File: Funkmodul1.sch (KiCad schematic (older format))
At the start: 54 parts, among them Q1 SSM3J334RLFTR-ND, Q17 AO3414, Q2 AO3414, U1 MC74HC4538A, U2 MAX892, U3 ATMEGA128-16AU, Y1 407F39D007M3728

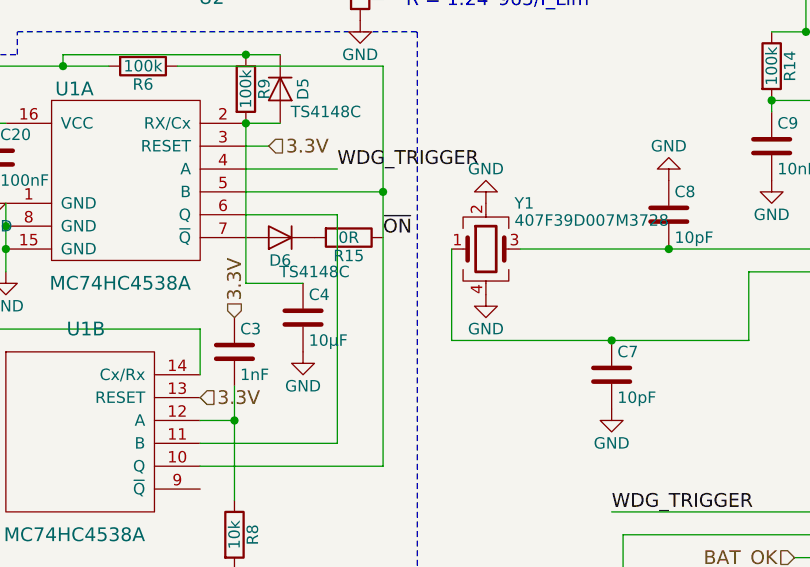
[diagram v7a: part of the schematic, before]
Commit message: Bugfix for external watchdog circuit
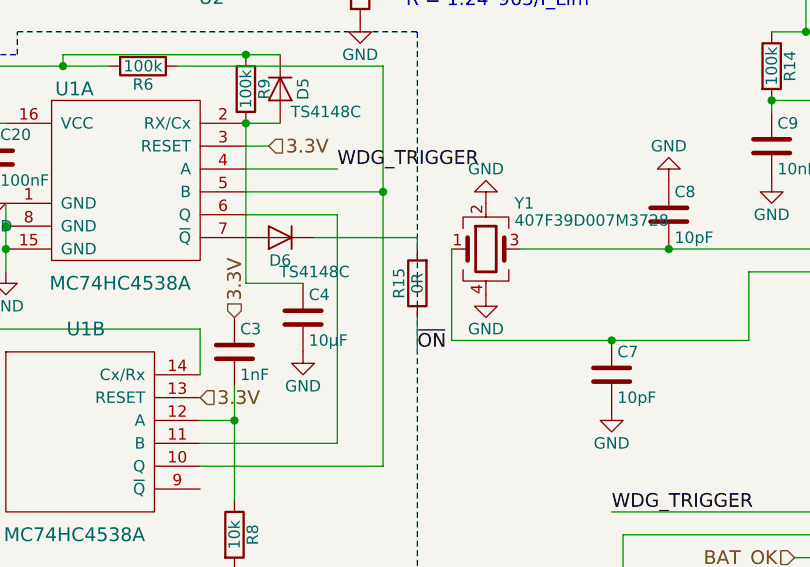
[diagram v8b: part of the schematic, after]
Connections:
- net ~ON~: no longer R6.1, U1.10 (Q), U1.5 (B)
- new net: R6.1, U1.10 (Q), U1.5 (B)
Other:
- moved on the sheet: R15
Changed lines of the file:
@@
 LIBS:contrib
 LIBS:valves
+LIBS:nxp-ic
+LIBS:7400-ic
 LIBS:cubesatFunkmodul-cache
 LIBS:funkmodul
+LIBS:CubeSat-Bus-1
+LIBS:CubeSat-Bus-2
 LIBS:disco-con
 LIBS:fiducial
@@
 Text HLabel 8150 5100 2    60   Input ~ 0
 RESET_3V3
-Text Label 3300 2600 0    60   ~ 0
+Text Label 3450 3100 0    60   ~ 0
 ~ON~
 $Comp
 L R R15
 U 1 1 5A0FBAB8
-P 3150 2600
-F 0 "R15" V 3230 2600 50  0000 C CNN
-F 1 "0R" V 3150 2600 50  0000 C CNN
-F 2 "Resistors_SMD:R_0805_HandSoldering" V 3080 2600 50  0001 C CNN
-F 3 "" H 3150 2600 50  0001 C CNN
-	1    3150 2600
-	0    1    1    0
-$EndComp
+P 3450 2800
+F 0 "R15" V 3530 2800 50  0000 C CNN
+F 1 "0R" V 3450 2800 50  0000 C CNN
+F 2 "Resistors_SMD:R_0805_HandSoldering" V 3380 2800 50  0001 C CNN
+F 3 "" H 3450 2800 50  0001 C CNN
+	1    3450 2800
+	-1   0    0    1
+$EndComp
+Wire Wire Line
+	3450 2950 3450 3100
+Wire Wire Line
+	3450 2650 3450 2600
+Wire Wire Line
+	3450 2600 3000 2600
 $EndSCHEMATC
